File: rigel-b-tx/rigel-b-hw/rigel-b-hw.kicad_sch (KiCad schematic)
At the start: 59 parts, among them IC1 BALFHB-WL-02D3, J1 Conn_01x03_Pin, J3 Conn_01x03_Pin, J4 BCS-102-L-D-TE, J5 S2B-XH-A, U1 STM32WLE5C8Ux, U2 TPS629206DRLR, U3 CH340X, U4 TYPE-C_16PIN_2MD(073), U5 X1G004131004200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

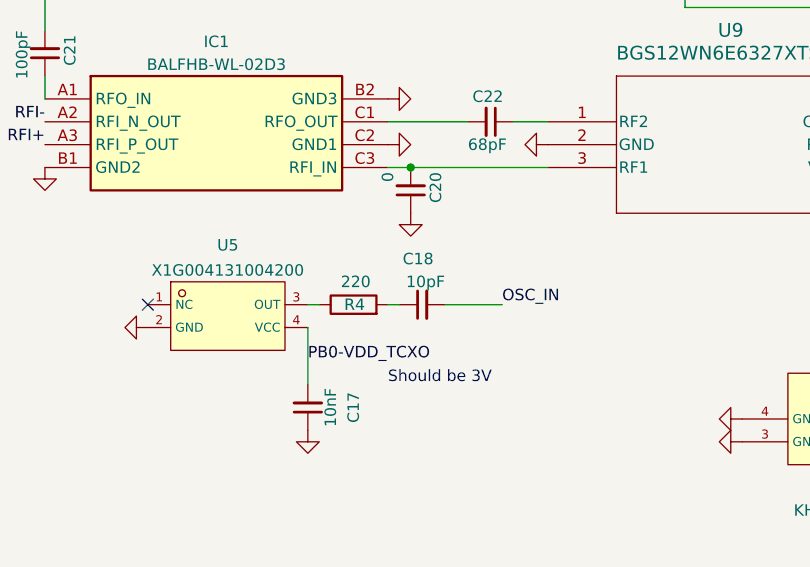
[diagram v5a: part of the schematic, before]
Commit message: PCB Layout ALMOST done
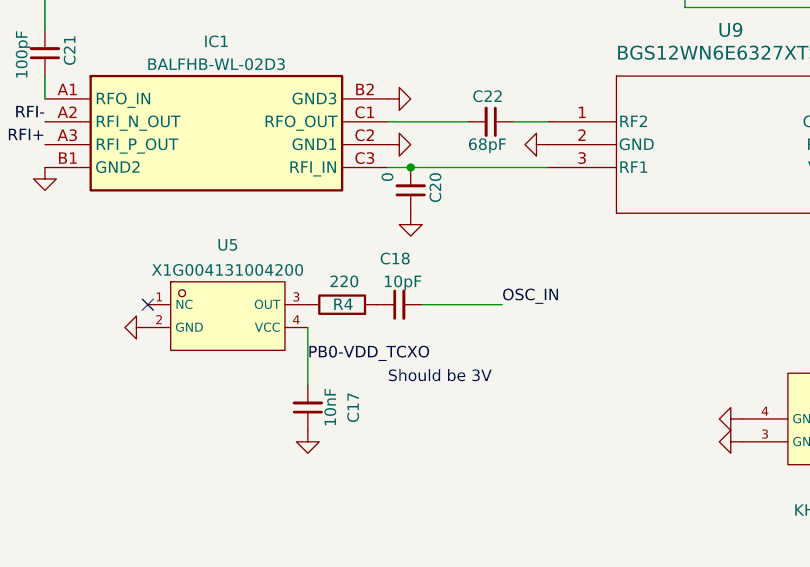
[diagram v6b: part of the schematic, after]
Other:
- moved on the sheet: C18, R4
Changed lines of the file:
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@@
 	(wire
 		(pts
-			(xy 55.88 102.87) (xy 57.15 102.87)
-		)
-		(stroke
-			(width 0)
-			(type default)
-		)
-	)
-	(wire
-		(pts
 			(xy 138.43 166.37) (xy 138.43 152.4)
 		)
@@
 	(wire
 		(pts
-			(xy 46.99 102.87) (xy 48.26 102.87)
-		)
-		(stroke
-			(width 0)
-			(type default)
-		)
-	)
-	(wire
-		(pts
 			(xy 264.16 132.08) (xy 260.35 132.08)
 		)
@@
 	(wire
 		(pts
-			(xy 62.23 102.87) (xy 68.58 102.87)
+			(xy 59.69 102.87) (xy 68.58 102.87)
 		)
 		(stroke
@@
 	(symbol
 		(lib_id "Device:R")
-		(at 52.07 102.87 90)
+		(at 50.8 102.87 90)
 		(unit 1)
 		(exclude_from_sim no)
@@
 		(dnp no)
 		(property "Reference" "R4"
-			(at 53.34 102.87 90)
+			(at 52.07 102.87 90)
 			(effects
 				(font
@@
 		)
 		(property "Value" "220"
-			(at 53.975 100.33 90)
+			(at 52.705 100.33 90)
 			(effects
 				(font
@@
 		)
 		(property "Footprint" "Resistor_SMD:R_0402_1005Metric"
-			(at 52.07 104.648 90)
+			(at 50.8 104.648 90)
 			(effects
 				(font
@@
 		)
 		(property "Datasheet" "~"
-			(at 52.07 102.87 0)
+			(at 50.8 102.87 0)
 			(effects
 				(font
@@
 		)
 		(property "Description" ""
-			(at 52.07 102.87 0)
+			(at 50.8 102.87 0)
 			(effects
 				(font
@@
 	(symbol
 		(lib_id "Device:C_Small")
-		(at 59.69 102.87 90)
+		(at 57.15 102.87 90)
 		(unit 1)
 		(exclude_from_sim no)
@@
 		(dnp no)
 		(property "Reference" "C18"
-			(at 60.96 97.79 90)
+			(at 58.42 97.79 90)
 			(effects
 				(font
@@
 		)
 		(property "Value" "10pF"
-			(at 62.23 100.33 90)
+			(at 59.69 100.33 90)
 			(effects
 				(font
@@
 		)
 		(property "Footprint" "Capacitor_SMD:C_0402_1005Metric"
-			(at 59.69 102.87 0)
+			(at 57.15 102.87 0)
 			(effects
 				(font
@@
 		)
 		(property "Datasheet" "~"
-			(at 59.69 102.87 0)
+			(at 57.15 102.87 0)
 			(effects
 				(font
@@
 		)
 		(property "Description" ""
-			(at 59.69 102.87 0)
+			(at 57.15 102.87 0)
 			(effects
 				(font

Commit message: PCB Layout
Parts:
- removed J1, J3: Conn_01x03_Pin, Connector_PinSocket_2.54mm:PinSocket_1x03_P2.54mm_Vertical, symbol Connector:Conn_01x03_Pin
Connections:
- net USART1_RX: now also U8.13 (TXD)
- net USART1_TX: now also U8.14 (RXD)
- net JTCK/SWCLK: no longer names the net of U1.42 (PA14)
- net JTMS/SWDIO: no longer names the net of U1.36 (PA13)
- no-connect marks 33 -> 35

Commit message: RF Switch finalized
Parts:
- removed U9: BGS12WN6E6327XTSA1, jlc:PG-TSNP-6-10_INF, symbol 2024-11-10_21-59-30:BGS12WN6E6327XTSA1
- added U9: PE42520C-Z, QFN_2520C-Z_PSM, symbol 2025-02-07_21-48-15:PE42520C-Z
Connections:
- net +3.3V: now also U9.16 (VDD)
- net GND: now also U9.1 (GND), U9.10 (GND), U9.12 (GND), U9.13 (VssEXT), U9.15 (LS), U9.17 (GND), U9.3 (GND), U9.4 (GND), U9.5 (GND), U9.6 (GND), U9.8 (GND), U9.9 (GND)
- net at C20.2, IC1.C3 (RFI_IN): now also U9.2 (RF1)
- net at C1.1: now also U9.7 (RFC)
- net at C22.1: now also U9.11 (RF2)
- net at U1.38 (PC13): now also U9.14 (CTRL)
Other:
- moved on the sheet: C1, C14, C15, C17, C18, C20, C21, C22, C24, IC1, J4, J5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
